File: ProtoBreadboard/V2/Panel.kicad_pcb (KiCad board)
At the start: 2 copper layers, 121.8 x 172.4 mm, 255 parts, among them IC1 AT90USB1286-AU, IC2 BSS138, IC3 BSS138, IC4 BSS138, IC5 BSS138, J1 Conn_01x30_Female, J10 Conn_01x04_Female, J11 Conn_01x32_Female, J12 Conn_01x06_Female, J13 Conn_01x08_Female, J14 Conn_01x08_Female, J15 Conn_01x04_Female, J16 Conn_01x03_Female, J17 Conn_01x03_Female, J18 Conn_01x07_Female, J19 Conn_01x02_Female, J2 Conn_01x10_Female, J20 Conn_01x02_Female, J21 Conn_01x02_Female, J22 AVR-ISP-6, J23 Conn_01x02_Female, J24 Conn_01x03_Female, J25 Conn_01x07_Female, J26 Conn_01x03_Female, J27 Conn_02x03_Counter_Clockwise, J28 Conn_01x03_Female, J29 Conn_01x02_Female, J3 Conn_01x32_Female, J30 Conn_01x02_Female, J31 Conn_01x02_Female, J32 Conn_01x02_Female, J33 Conn_01x10_Female, J34 Conn_01x10_Female, J35 Conn_01x10_Female, J36 Conn_01x10_Female, J37 Conn_01x10_Female, J38 Conn_01x10_Female, J39 Conn_01x10_Female, J4 Conn_01x10_Female, J40 Conn_01x10_Female, J41 Conn_01x10_Female, J42 Conn_01x10_Female, J43 Conn_01x10_Female, J44 Conn_01x10_Female, J45 Conn_01x10_Female, J46 Conn_01x10_Female, J47 Conn_01x10_Female, J48 Conn_01x10_Female, J49 Conn_01x10_Female, J5 Conn_01x30_Female, J50 Conn_01x10_Female, J51 Conn_01x03_Female, J52 Conn_01x02_Female, J53 Conn_01x04_Female, J54 Conn_01x02_Female, J55 Conn_01x02_Female, J56 Conn_01x02_Female, J57 Conn_01x02_Female, J58 Conn_01x02_Female, J6 Conn_01x02_Female, J7 Conn_01x02_Female, J8 Conn_01x06_Female, J9 Conn_01x04_Female, SW1 RotaryEncoder_Switch, SW2 RotaryEncoder_Switch, U1 IS31FL3741A, U2 AP2112K-3.3, U3 PRTR5V0U2X, U4 AP2112K-3.3, Y1 Crystal, Y2 Crystal, Y3 Crystal

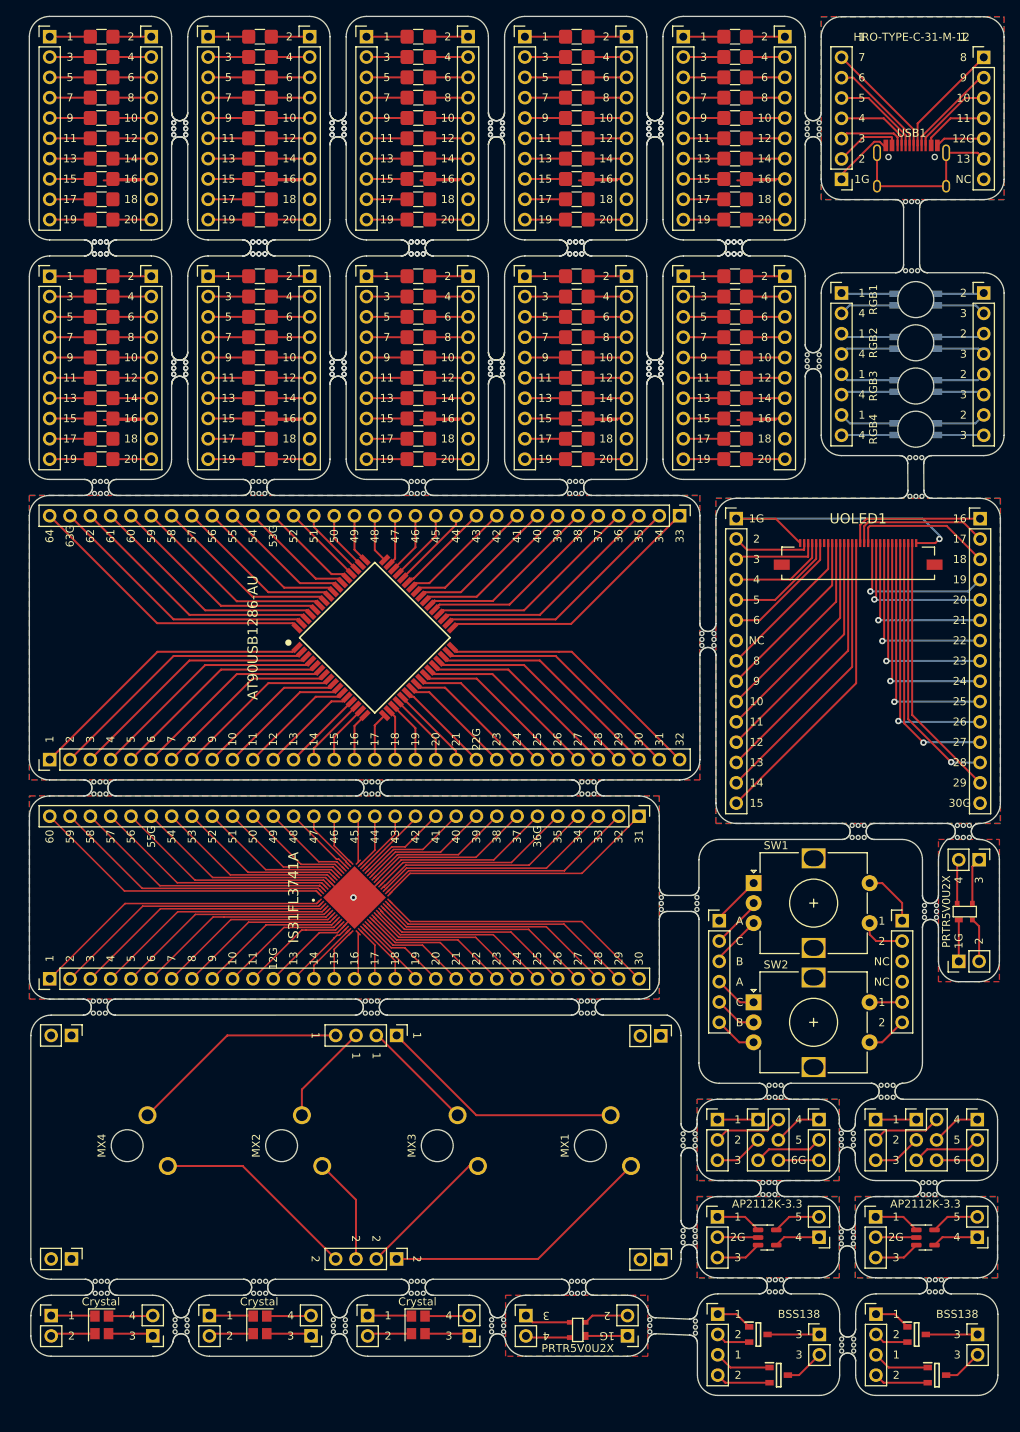
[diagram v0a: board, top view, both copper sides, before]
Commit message: Main Panel Gerber for Stencil
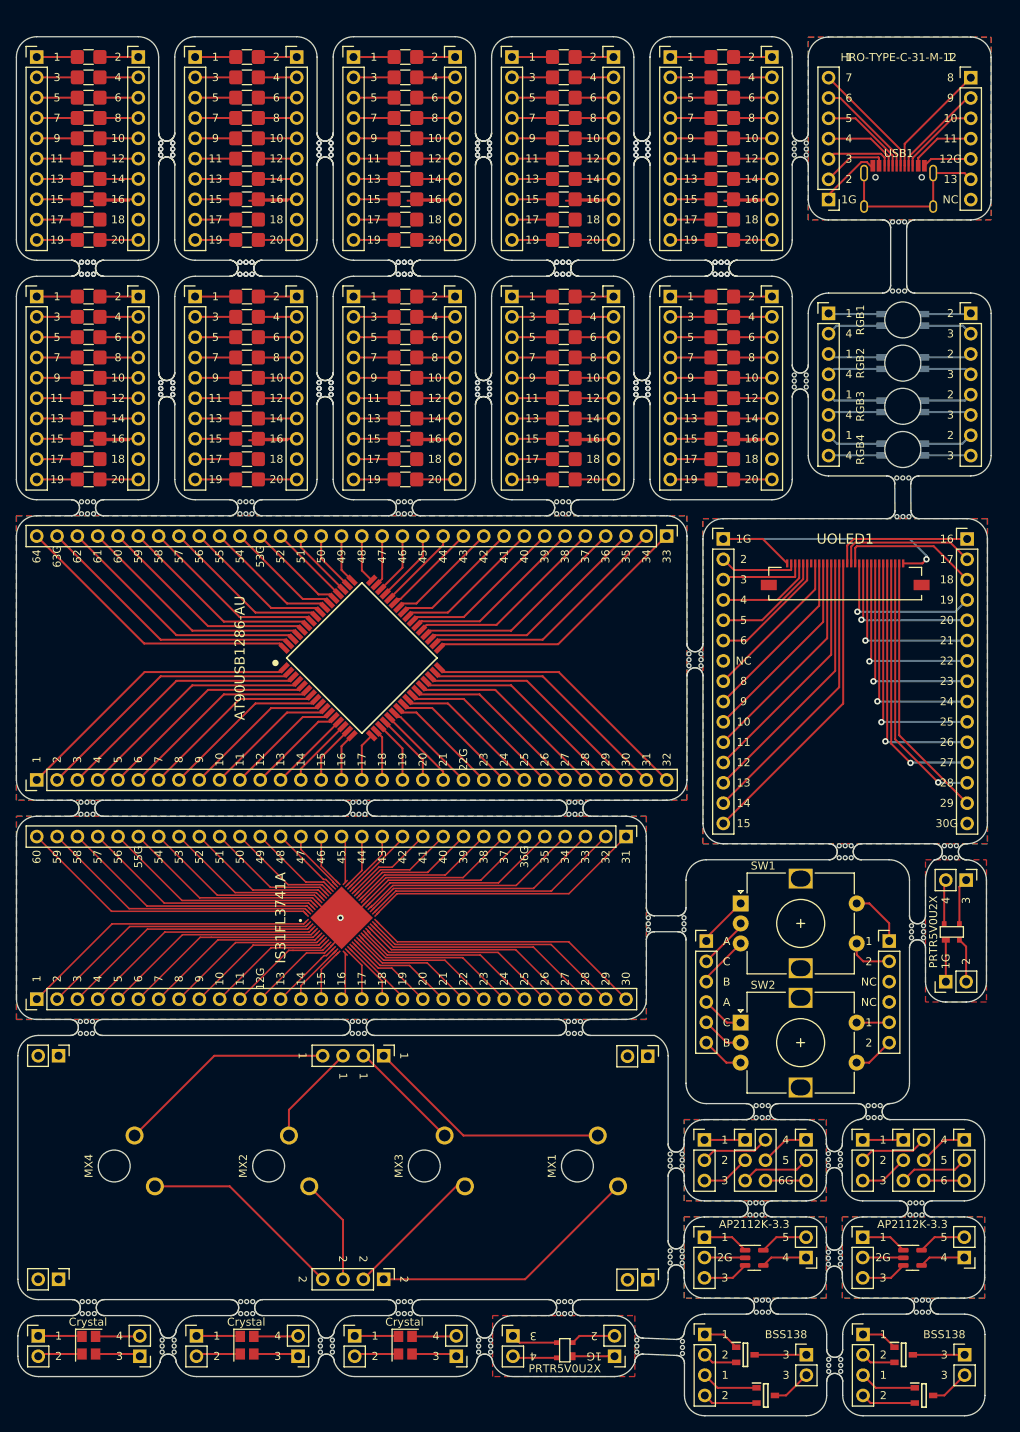
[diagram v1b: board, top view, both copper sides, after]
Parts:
- moved U2 3.01 mm to (153.0, 188.4)
- moved U4 3.01 mm to (172.8, 188.4)
- moved mouse-bite-2mm-slot 3.01 mm to (168.0, 170.1)
- moved mouse-bite-2mm-slot 3.01 mm to (173.2, 182.2)
- moved mouse-bite-2mm-slot 3.01 mm to (153.2, 182.2)
- moved mouse-bite-2mm-slot 3.01 mm to (154.0, 170.1)
- moved mouse-bite-2mm-slot 3.01 mm to (163.1, 201.8)
- moved J1 3.01 mm to (63.3, 156.0)
- moved G53 3.01 mm to (69.8, 73.3)
- moved G55 3.01 mm to (69.8, 78.4)
- moved G57 3.01 mm to (69.8, 83.4)
- moved G83 3.01 mm to (129.2, 73.3)
- moved G85 3.01 mm to (129.2, 78.4)
- moved G87 3.01 mm to (129.2, 83.4)
- moved J11 3.01 mm to (142.1, 98.1)
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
